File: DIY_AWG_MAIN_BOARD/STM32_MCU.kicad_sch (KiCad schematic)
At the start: 41 parts, among them J2 Conn_01x04_Pin, J3 Conn_01x02_Pin, SW1 SW_Push, SW2 SW_Push, SW3 SW_Push, SW4 SW_Push, U10 STM32G473VETx, U8 USBLC6-2SC6, U9 161N-4BVS11, X1 SX2M8.000B10F20TNN

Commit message: Updated main PCB, daughter PCB
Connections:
- net +3V3: no longer FPC1.1, FPC1.2, FPC1.3
- net +VSW5V0: now also FPC1.1, FPC1.2, FPC1.3
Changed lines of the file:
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@@
+	)
+	(symbol
+		(lib_id "power:+3.3V")
+		(at 295.91 72.39 270)
+		(unit 1)
+		(body_style 1)
+		(exclude_from_sim no)
+		(in_bom yes)
+		(on_board yes)
+		(in_pos_files yes)
+		(dnp no)
+		(property "Reference" "#PWR0218"
+			(at 292.1 72.39 0)
+			(hide yes)
+			(show_name no)
+			(do_not_autoplace no)
+			(effects
+				(font
+					(size 1.27 1.27)
+				)
+			)
+		)
+		(property "Value" "+VSW5V0"
+			(at 303.276 72.39 90)
+			(show_name no)
+			(do_not_autoplace no)
+			(effects
+				(font
+					(size 1.27 1.27)
+				)
+			)
+		)
+		(property "Footprint" ""
+			(at 295.91 72.39 0)
+			(hide yes)
+			(show_name no)
+			(do_not_autoplace no)
+			(effects
+				(font
+					(size 1.27 1.27)
+				)
+			)
+		)
+		(property "Datasheet" ""
+			(at 295.91 72.39 0)
+			(hide yes)
+			(show_name no)
+			(do_not_autoplace no)
+			(effects
+				(font
+					(size 1.27 1.27)
+				)
+			)
+		)
+		(property "Description" "Power symbol creates a global label with name \"+3.3V\""
+			(at 295.91 72.39 0)
+			(hide yes)
+			(show_name no)
+			(do_not_autoplace no)
+			(effects
+				(font
+					(size 1.27 1.27)
+				)
+			)
+		)
+		(pin "1"
+		)
+		(instances
+			(project "DIY_AWG_V1.1"
+				(path "/508078af-d961-4af3-840e-a064a9f8d5bc/aaba8d51-2713-41de-9761-99ebb3cee83e"
+					(reference "#PWR0218")
+					(unit 1)
+				)
+			)
+		)
 	)
 	(symbol
@@
 					(unit 1)
 				)
-			)
-		)
-	)
-	(symbol
-		(lib_id "power:+3V3")
-		(at 295.91 72.39 270)
-		(unit 1)
-		(body_style 1)
-		(exclude_from_sim no)
-		(in_bom yes)
-		(on_board yes)
-		(in_pos_files yes)
-		(dnp no)
-		(fields_autoplaced yes)
-		(property "Reference" "#PWR0109"
-			(at 292.1 72.39 0)
-			(hide yes)
-			(show_name no)
-			(do_not_autoplace no)
-			(effects
-				(font
-					(size 1.27 1.27)
-				)
-			)
-		)
-		(property "Value" "+3V3"
-			(at 299.72 72.3899 90)
-			(show_name no)
-			(do_not_autoplace no)
-			(effects
-				(font
-					(size 1.27 1.27)
-				)
-				(justify left)
-			)
-		)
-		(property "Footprint" ""
-			(at 295.91 72.39 0)
-			(hide yes)
-			(show_name no)
-			(do_not_autoplace no)
-			(effects
-				(font
-					(size 1.27 1.27)
-				)
-			)
-		)
-		(property "Datasheet" ""
-			(at 295.91 72.39 0)
-			(hide yes)
-			(show_name no)
-			(do_not_autoplace no)
-			(effects
-				(font
-					(size 1.27 1.27)
-				)
-			)
-		)
-		(property "Description" "Power symbol creates a global label with name \"+3V3\""
-			(at 295.91 72.39 0)
-			(hide yes)
-			(show_name no)
-			(do_not_autoplace no)
-			(effects
-				(font
-					(size 1.27 1.27)
-				)
-			)
-		)
-		(pin "1"
-		)
-		(instances
-			(project "DIY_AWG_V1.1"
-				(path "/508078af-d961-4af3-840e-a064a9f8d5bc/aaba8d51-2713-41de-9761-99ebb3cee83e"
-					(reference "#PWR0109")
-					(unit 1)
-				)

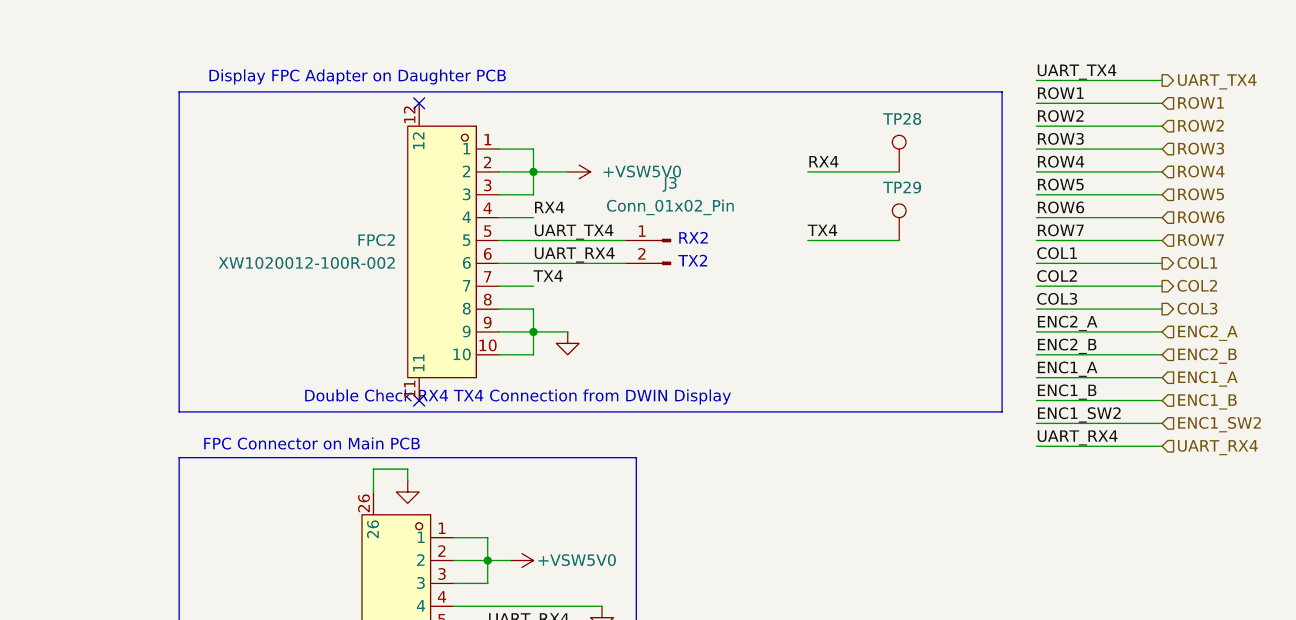
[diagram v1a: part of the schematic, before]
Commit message: Updated daughter board and main board PCB design schematics
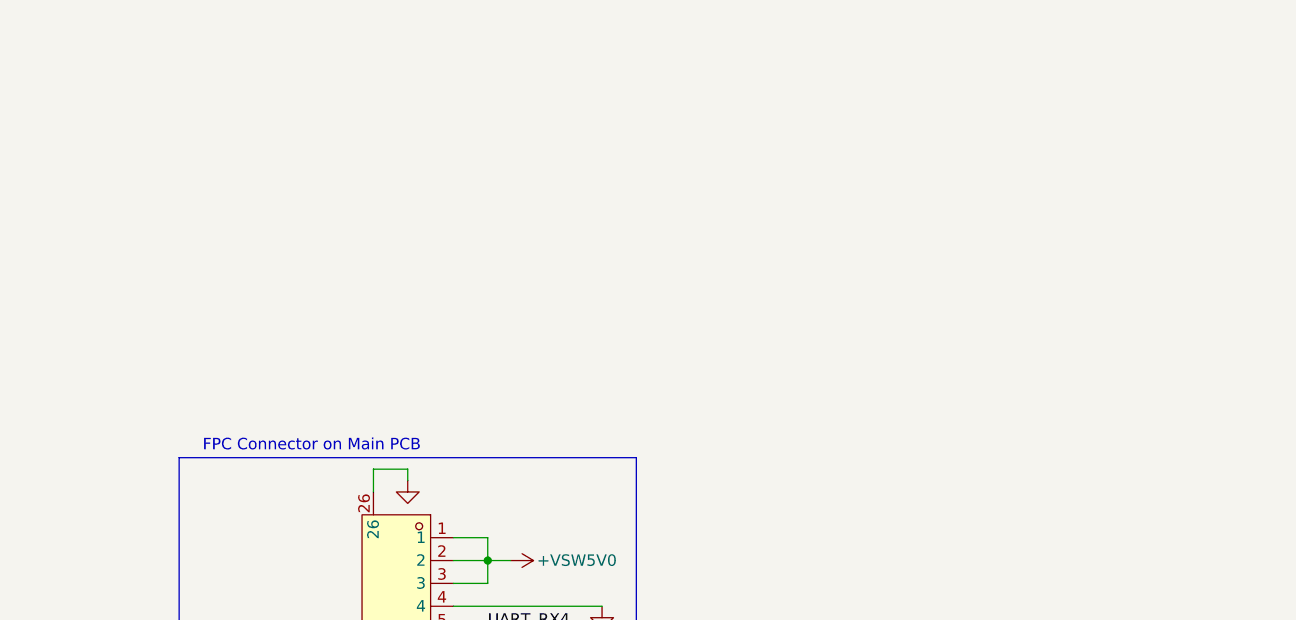
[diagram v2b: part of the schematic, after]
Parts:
- removed FPC2: XW1020012-100R-002, easyeda2kicad:FPC-SMD_10P-P1.00_XW1020012-100R-001, symbol easyeda2kicad:XW1020012-100R-002
- removed J3: Conn_01x02_Pin, Connector_PinHeader_2.54mm:PinHeader_1x02_P2.54mm_Vertical, symbol Connector:Conn_01x02_Pin
- removed TP28, TP29: TestPoint, TestPoint:TestPoint_Pad_D1.0mm, symbol Connector:TestPoint
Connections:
- no-connect marks 49 -> 47
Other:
- note removed: "Display FPC Adapter on Daughter PCB"
- note removed: "Double Check RX4 TX4 Connection from DWIN Display"
- note removed: "RX2"
- note removed: "TX2"

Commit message: Updated main board schematic and design
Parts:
- C42: value 4.7n -> 100n; footprint Capacitor_SMD:C_0402_1005Metric -> Capacitor_SMD:C_0603_1608Metric; Component Name 04023C472KAT2A -> C0603C104J3RACTU; LCSC ID C5128374 -> C2167388
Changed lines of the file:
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@@
 	)
 	(junction
-		(at 156.21 27.94)
+		(at 95.25 27.94)
 		(diameter 0)
 		(color 0 0 0 0)
 	)
 	(junction
-		(at 95.25 27.94)
+		(at 274.32 208.28)
 		(diameter 0)
 		(color 0 0 0 0)
 	)
 	(junction
-		(at 274.32 208.28)
+		(at 156.21 27.94)
 		(diameter 0)
 		(color 0 0 0 0)
@@
 	(wire
 		(pts
+			(xy 156.21 27.94) (xy 166.37 27.94)
+		)
+		(stroke
+			(width 0)
+			(type default)
+		)
+	)
+	(wire
+		(pts
 			(xy 289.56 102.87) (xy 293.37 102.87)
 		)
@@
 	(wire
 		(pts
-			(xy 156.21 27.94) (xy 166.37 27.94)
-		)
-		(stroke
-			(width 0)
-			(type default)
-		)
-	)
-	(wire
-		(pts
 			(xy 48.26 46.99) (xy 109.22 46.99)
 		)
@@
 	)
 	(symbol
+		(lib_id "Device:C")
+		(at 156.21 31.75 0)
+		(unit 1)
+		(body_style 1)
+		(exclude_from_sim no)
+		(in_bom yes)
+		(on_board yes)
+		(in_pos_files yes)
+		(dnp no)
+		(property "Reference" "C42"
+			(at 159.004 30.48 0)
+			(show_name no)
+			(do_not_autoplace no)
+			(effects
+				(font
+					(size 1.27 1.27)
+				)
+				(justify left)
+			)
+		)
+		(property "Value" "100n"
+			(at 158.75 33.02 0)
+			(show_name no)
+			(do_not_autoplace no)
+			(effects
+				(font
+					(size 1.27 1.27)
+				)
+				(justify left)
+			)
+		)
+		(property "Footprint" "Capacitor_SMD:C_0603_1608Metric"
+			(at 157.1752 35.56 0)
+			(hide yes)
+			(show_name no)
+			(do_not_autoplace no)
+			(effects
+				(font
+					(size 1.27 1.27)
+				)
+			)
+		)
+		(property "Datasheet" "https://www.lcsc.com/datasheet/C2167388.pdf?spm=wm.sxq.inf.ggs___wm.fly.bg.0.xh&lcsc_vid=EVldUV1eRAJaUwYHFAdaVVJVQFRYUFFWFAdfXgVUElQxVlNeQlNWXlZRRVVYUjsOAxUeFF5JWBYZEEoKFBINSQcJGk4eFQsCAgIaSgADAwAHC0slRFBXUFRXWQkaCgg%3D"
+			(at 156.21 31.75 0)
+			(hide yes)
+			(show_name no)
+			(do_not_autoplace no)
+			(effects
+				(font
+					(size 1.27 1.27)
+				)
+			)
+		)
+		(property "Description" "Unpolarized capacitor"
+			(at 156.21 31.75 0)
+			(hide yes)
+			(show_name no)
+			(do_not_autoplace no)
+			(effects
+				(font
+					(size 1.27 1.27)
+				)
+			)
+		)
+		(property "Component Name" "C0603C104J3RACTU"
+			(at 157.734 37.084 0)
+			(show_name no)
+			(do_not_autoplace no)
+			(effects
+				(font
+					(size 1.27 1.27)
+				)
+			)
+		)
+		(property "LCSC ID" "C2167388"
+			(at 156.21 31.75 0)
+			(hide yes)
+			(show_name no)
+			(do_not_autoplace no)
+			(effects
+				(font
+					(size 1.27 1.27)
+				)
+			)
+		)
+		(pin "1"
+		)
+		(pin "2"
+		)
+		(instances
+			(project "DIY_AWG_V1.1"
+				(path "/508078af-d961-4af3-840e-a064a9f8d5bc/aaba8d51-2713-41de-9761-99ebb3cee83e"
+					(reference "C42")
+					(unit 1)
+				)
+			)
+		)
+	)
+	(symbol
 		(lib_id "power:+3.3V")
 		(at 353.06 160.02 270)
@@
 					(unit 1)
 				)
-			)
-		)
-	)
-	(symbol
-		(lib_id "Device:C")
-		(at 156.21 31.75 0)
-		(unit 1)
-		(body_style 1)
-		(exclude_from_sim no)
-		(in_bom yes)
-		(on_board yes)
-		(in_pos_files yes)
-		(dnp no)
-		(property "Reference" "C42"
-			(at 159.004 30.48 0)
-			(show_name no)
-			(do_not_autoplace no)
-			(effects
-				(font
-					(size 1.27 1.27)
-				)
-				(justify left)
-			)
-		)
-		(property "Value" "4.7n"
-			(at 159.258 33.02 0)
-			(show_name no)
-			(do_not_autoplace no)
-			(effects
-				(font
-					(size 1.27 1.27)
-				)
-				(justify left)
-			)
-		)
-		(property "Footprint" "Capacitor_SMD:C_0402_1005Metric"
-			(at 157.1752 35.56 0)
-			(hide yes)
-			(show_name no)
-			(do_not_autoplace no)
-			(effects
-				(font
-					(size 1.27 1.27)
-				)
-			)
-		)
-		(property "Datasheet" "https://datasheets.kyocera-avx.com/KGM_X7R.pdf"
-			(at 156.21 31.75 0)
-			(hide yes)
-			(show_name no)
-			(do_not_autoplace no)
-			(effects
-				(font
-					(size 1.27 1.27)
-				)
-			)
-		)
-		(property "Description" "Unpolarized capacitor"
-			(at 156.21 31.75 0)
-			(hide yes)
-			(show_name no)
-			(do_not_autoplace no)
-			(effects
-				(font
-					(size 1.27 1.27)
-				)
-			)
-		)
-		(property "Component Name" "04023C472KAT2A"
-			(at 158.75 26.67 0)
-			(hide yes)
-			(show_name no)
-			(do_not_autoplace no)
-			(effects
-				(font
-					(size 1.27 1.27)
-				)
-			)
-		)
-		(property "LCSC ID" "C5128374"
-			(at 156.21 31.75 0)
-			(hide yes)
-			(show_name no)
-			(do_not_autoplace no)
-			(effects
-				(font
-					(size 1.27 1.27)
-				)
-			)
-		)
-		(pin "2"
-		)
-		(pin "1"
-		)
-		(instances
-			(project "DIY_AWG_V1.1"
-				(path "/508078af-d961-4af3-840e-a064a9f8d5bc/aaba8d51-2713-41de-9761-99ebb3cee83e"
-					(reference "C42")
-					(unit 1)
-				)
